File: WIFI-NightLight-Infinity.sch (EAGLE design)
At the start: 34 parts, among them CN1 PBS-3-VERTICAL, CN2 PBS-2-VERTICAL, CN5 PBS-2-VERTICAL, CN6 PBS-2-VERTICAL, CN7 PBS-4-VERTICAL, IC3 MC34063AD, IC4 DS1307Z, M1 ESP8266-12F, Q1 32.768K

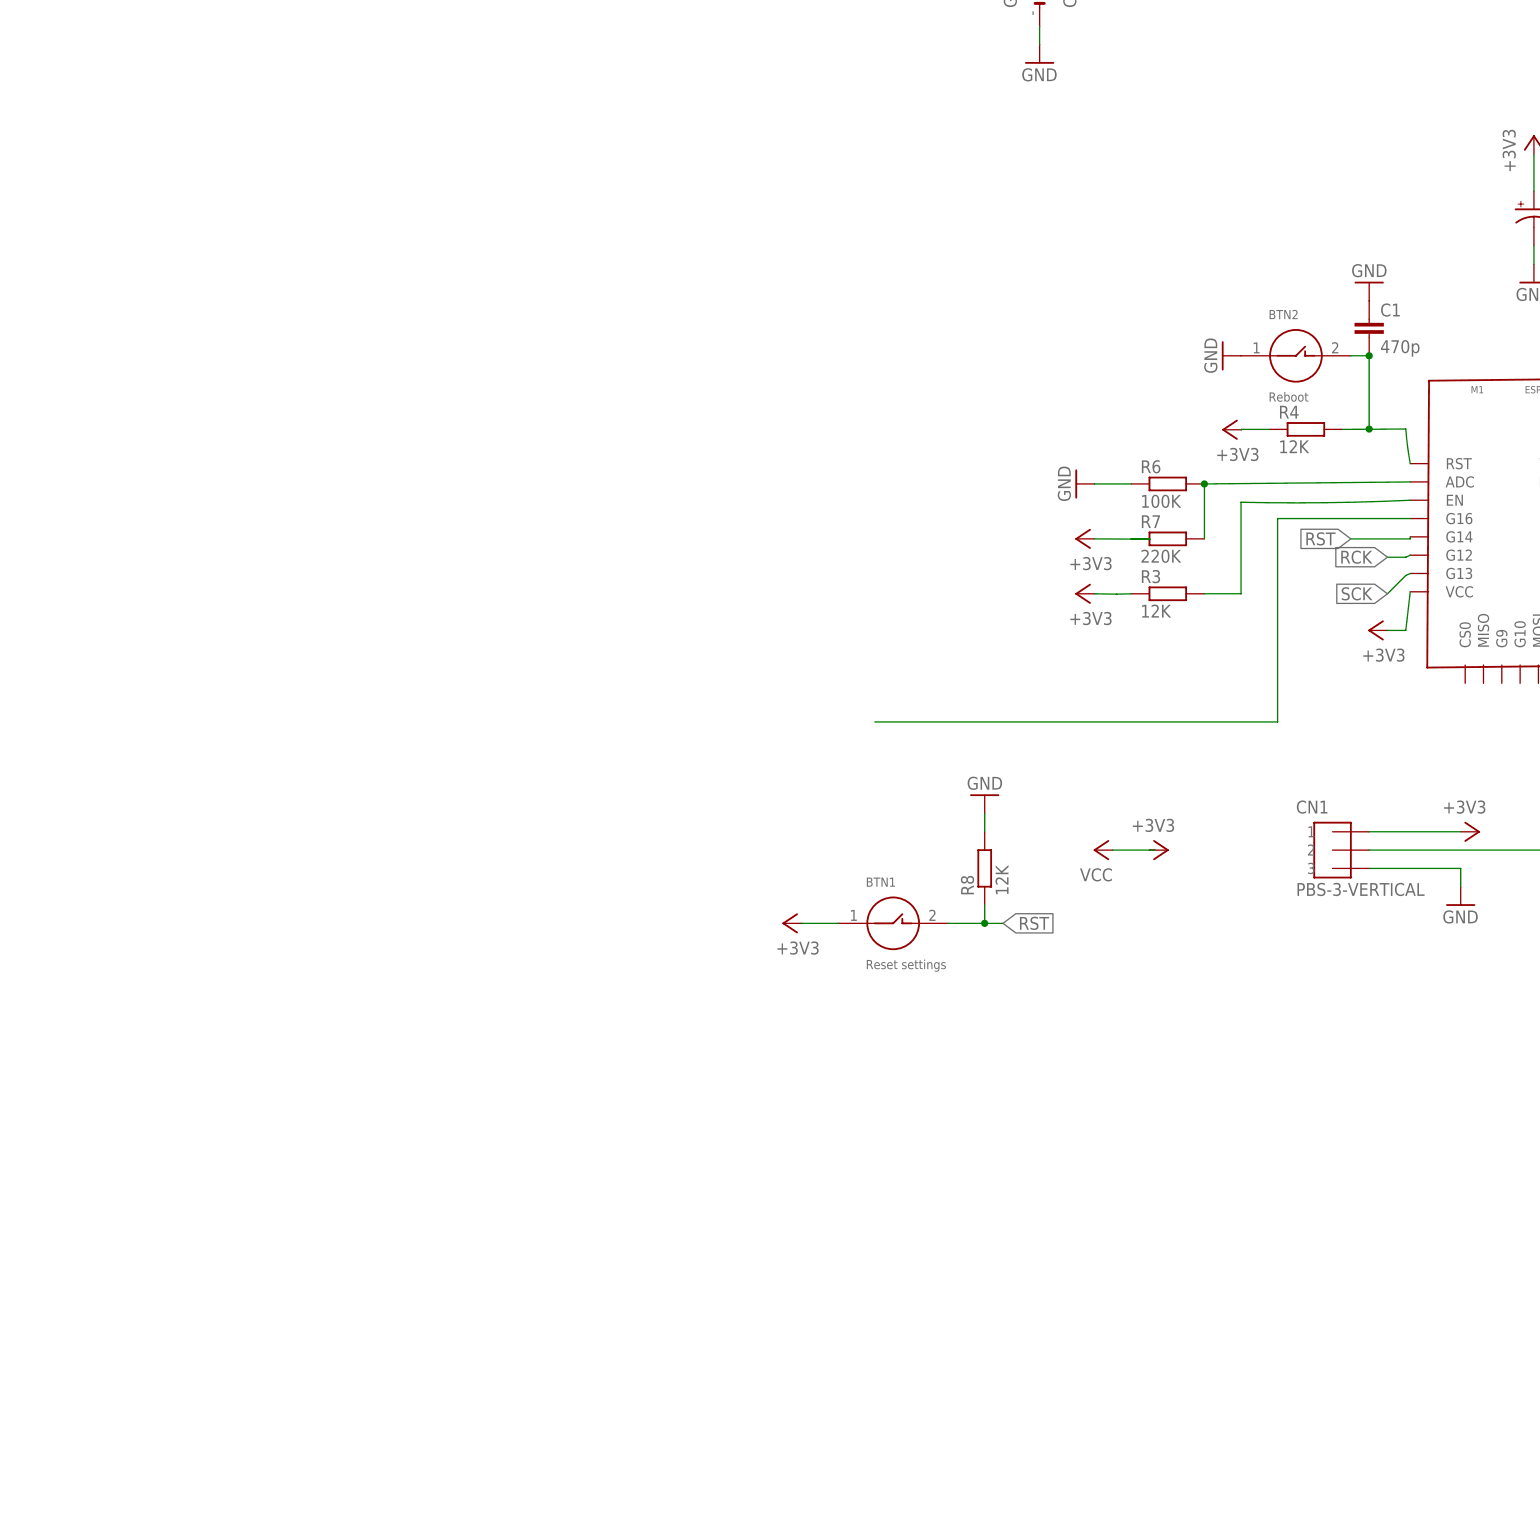
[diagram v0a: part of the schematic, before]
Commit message: transistors were aaded
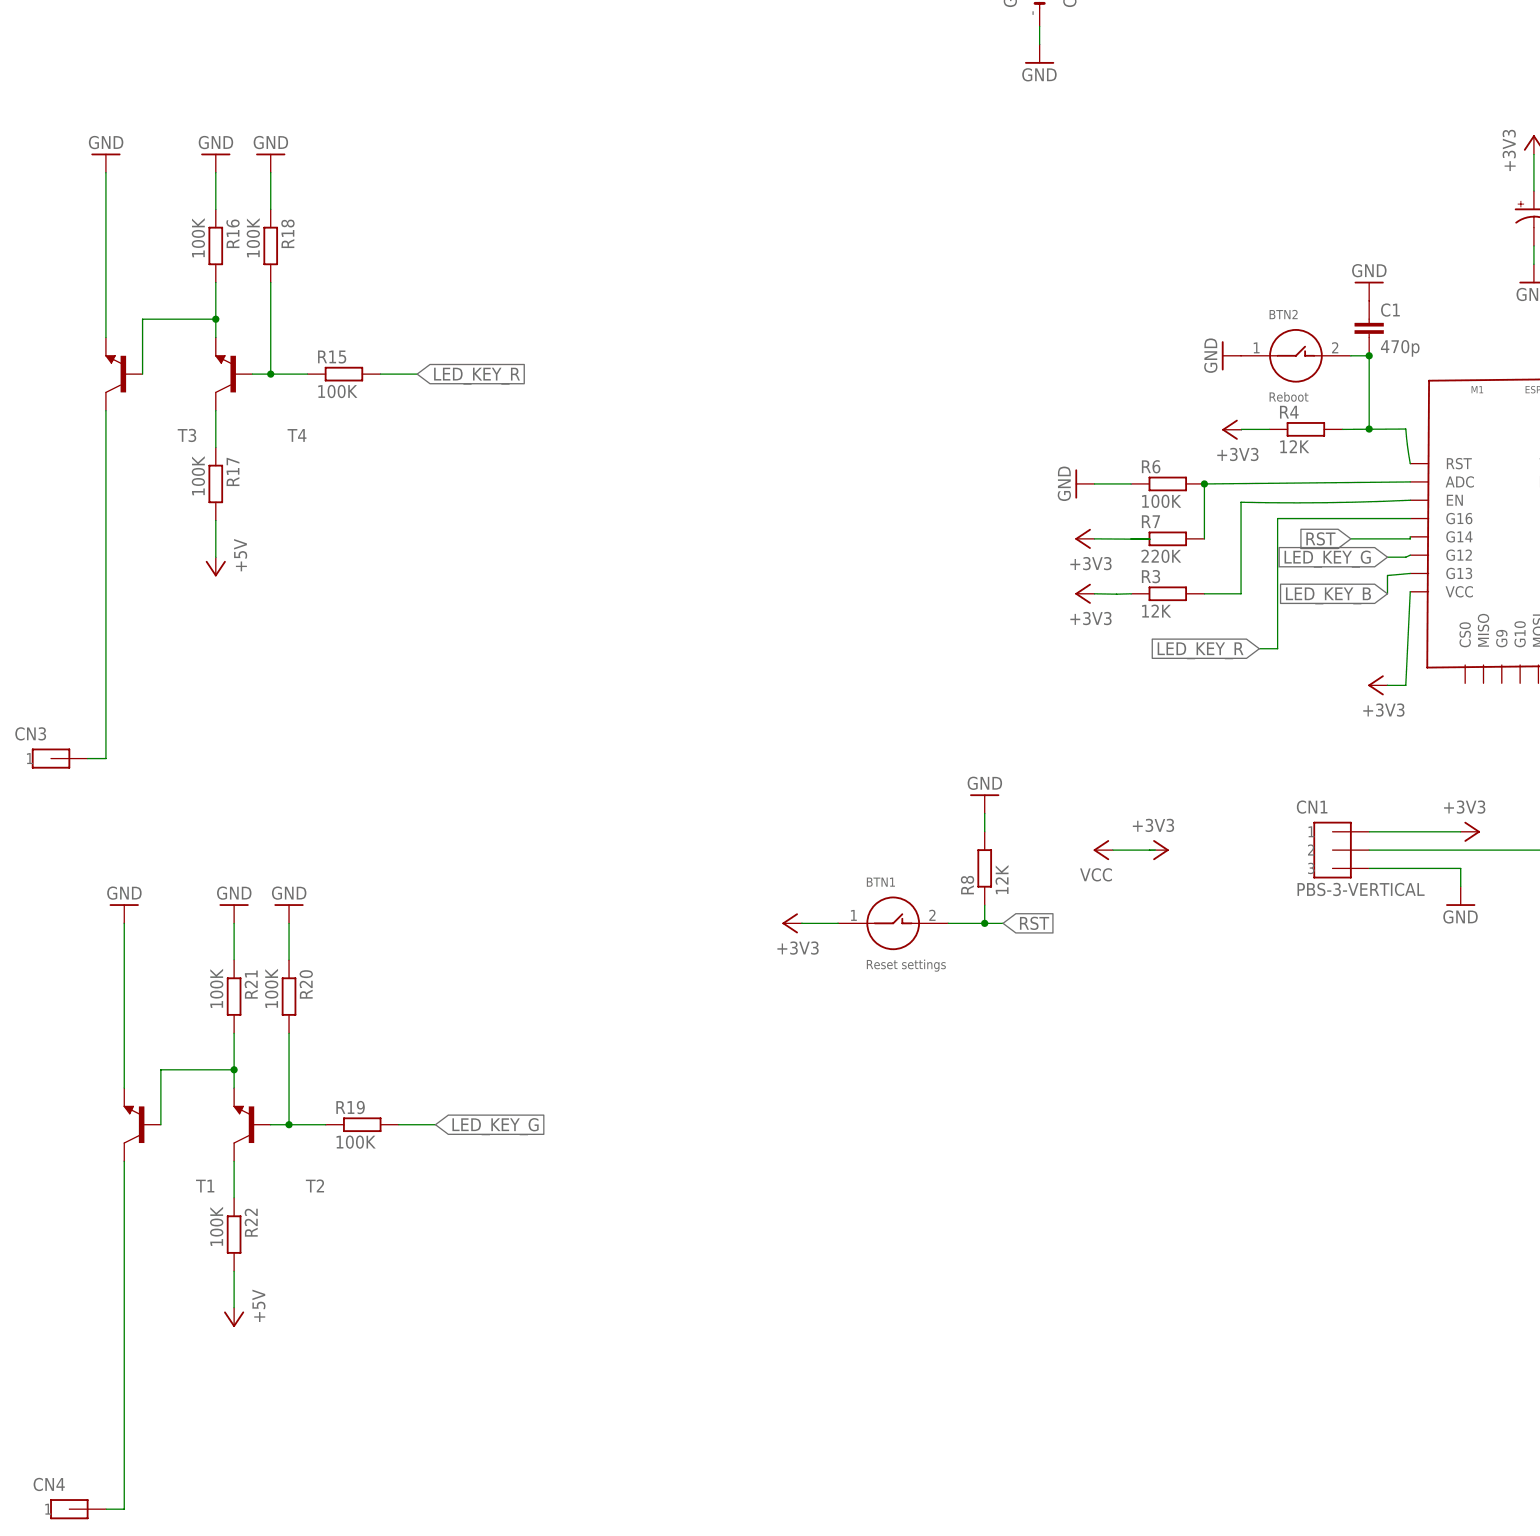
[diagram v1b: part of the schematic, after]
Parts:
- added CN3, CN4: (no value), pls:PBS-1-VERTICAL
- added R15, R16, R17, R18, R19, R20, R21, R22: 100K, eagle-ltspice:RR0603
- added T1, T2, T3, T4: (no value), transistor:-NPN-TO126V
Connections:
- net SCK renamed LED_KEY_B
- removed net N$27: M1.G16
- removed net RCK: M1.G12
- new net LED_KEY_G: M1.G12, R19.2
- new net LED_KEY_R: M1.G16, R15.2
- new net N$10: R17.1, T4.C
- new net N$11: R19.1, R20.2, T2.B
- new net N$12: CN3.1, T3.C
- new net N$13: R21.2, T1.B, T2.E
- new net N$14: R22.1, T2.C
- new net N$15: CN4.1, T1.C
- new net N$8: R15.1, R18.2, T4.B
- new net N$9: R16.2, T3.B, T4.E
- net +5V: now also R17.2, R22.2
- net GND: now also R16.1, R18.1, R20.1, R21.1, T1.E, T3.E

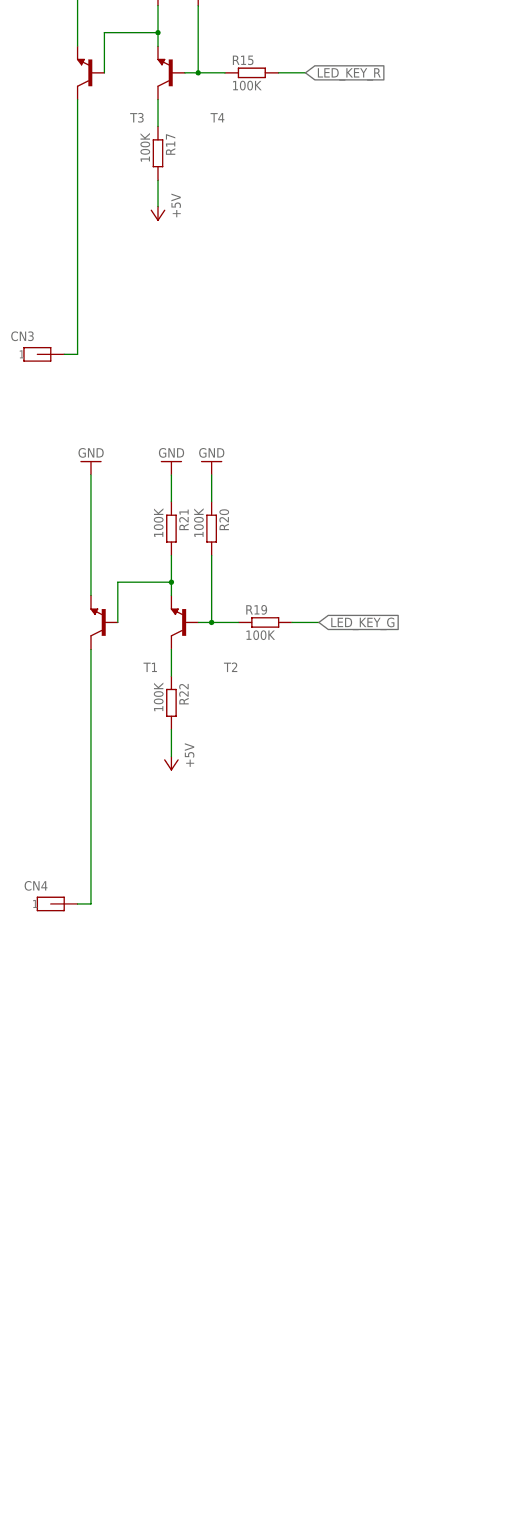
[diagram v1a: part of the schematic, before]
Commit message: Scheme for all led-channels have done
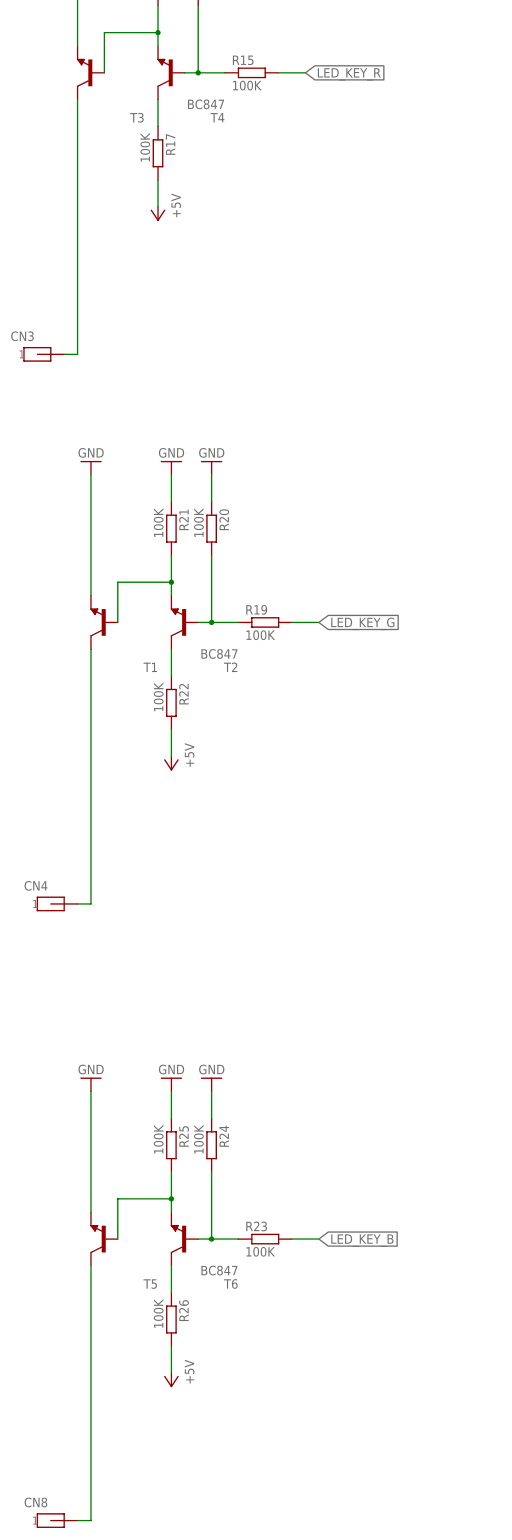
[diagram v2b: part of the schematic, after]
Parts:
- added CN8: (no value), pls:PBS-1-VERTICAL
- added R23, R24, R25, R26: 100K, eagle-ltspice:RR0603
- added T5: (no value), transistor:-NPN-TO126V
- added T6: BC847, transistor:BC847
- T2, T4: value (none) -> BC847; device transistor:-NPN-TO126V -> transistor:BC847
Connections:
- new net N$16: R23.1, R24.2, T6.B
- new net N$17: R25.2, T5.B, T6.E
- new net N$18: R26.1, T6.C
- new net N$19: CN8.1, T5.C
- net +5V: now also R26.2
- net GND: now also R24.1, R25.1, T5.E
- net LED_KEY_B: now also R23.2
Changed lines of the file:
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@@
 <part name="GND21" library="supply1" library_urn="urn:adsk.eagle:library:371" deviceset="GND" device=""/>
 <part name="T3" library="transistor" library_urn="urn:adsk.eagle:library:402" deviceset="*-NPN-" device="TO126V" package3d_urn="urn:adsk.eagle:package:29912/1"/>
-<part name="T4" library="transistor" library_urn="urn:adsk.eagle:library:402" deviceset="*-NPN-" device="TO126V" package3d_urn="urn:adsk.eagle:package:29912/1"/>
+<part name="T4" library="transistor" library_urn="urn:adsk.eagle:library:402" deviceset="BC847" device="" package3d_urn="urn:adsk.eagle:package:29904/2"/>
 <part name="R15" library="eagle-ltspice" library_urn="urn:adsk.eagle:library:217" deviceset="R" device="R0603" package3d_urn="urn:adsk.eagle:package:13302/1" value="100K"/>
 <part name="R18" library="eagle-ltspice" library_urn="urn:adsk.eagle:library:217" deviceset="R" device="R0603" package3d_urn="urn:adsk.eagle:package:13302/1" value="100K"/>
@@
 <part name="CN3" library="pls" deviceset="PBS-1-VERTICAL" device=""/>
 <part name="T1" library="transistor" library_urn="urn:adsk.eagle:library:402" deviceset="*-NPN-" device="TO126V" package3d_urn="urn:adsk.eagle:package:29912/1"/>
-<part name="T2" library="transistor" library_urn="urn:adsk.eagle:library:402" deviceset="*-NPN-" device="TO126V" package3d_urn="urn:adsk.eagle:package:29912/1"/>
+<part name="T2" library="transistor" library_urn="urn:adsk.eagle:library:402" deviceset="BC847" device="" package3d_urn="urn:adsk.eagle:package:29904/2"/>
 <part name="R19" library="eagle-ltspice" library_urn="urn:adsk.eagle:library:217" deviceset="R" device="R0603" package3d_urn="urn:adsk.eagle:package:13302/1" value="100K"/>
 <part name="R20" library="eagle-ltspice" library_urn="urn:adsk.eagle:library:217" deviceset="R" device="R0603" package3d_urn="urn:adsk.eagle:package:13302/1" value="100K"/>
@@
 <part name="P+4" library="supply1" library_urn="urn:adsk.eagle:library:371" deviceset="+5V" device=""/>
 <part name="CN4" library="pls" deviceset="PBS-1-VERTICAL" device=""/>
+<part name="T5" library="transistor" library_urn="urn:adsk.eagle:library:402" deviceset="*-NPN-" device="TO126V" package3d_urn="urn:adsk.eagle:package:29912/1"/>
+<part name="T6" library="transistor" library_urn="urn:adsk.eagle:library:402" deviceset="BC847" device="" package3d_urn="urn:adsk.eagle:package:29904/2"/>
+<part name="R23" library="eagle-ltspice" library_urn="urn:adsk.eagle:library:217" deviceset="R" device="R0603" package3d_urn="urn:adsk.eagle:package:13302/1" value="100K"/>
+<part name="R24" library="eagle-ltspice" library_urn="urn:adsk.eagle:library:217" deviceset="R" device="R0603" package3d_urn="urn:adsk.eagle:package:13302/1" value="100K"/>
+<part name="GND26" library="supply1" library_urn="urn:adsk.eagle:library:371" deviceset="GND" device=""/>
+<part name="GND27" library="supply1" library_urn="urn:adsk.eagle:library:371" deviceset="GND" device=""/>
+<part name="R25" library="eagle-ltspice" library_urn="urn:adsk.eagle:library:217" deviceset="R" device="R0603" package3d_urn="urn:adsk.eagle:package:13302/1" value="100K"/>
+<part name="GND28" library="supply1" library_urn="urn:adsk.eagle:library:371" deviceset="GND" device=""/>
+<part name="R26" library="eagle-ltspice" library_urn="urn:adsk.eagle:library:217" deviceset="R" device="R0603" package3d_urn="urn:adsk.eagle:package:13302/1" value="100K"/>
+<part name="P+6" library="supply1" library_urn="urn:adsk.eagle:library:371" deviceset="+5V" device=""/>
+<part name="CN8" library="pls" deviceset="PBS-1-VERTICAL" device=""/>
 </parts>
 <sheets>
@@
 <instance part="P+4" gate="1" x="-175.26" y="-114.3" rot="R180"/>
 <instance part="CN4" gate="G$1" x="-198.12" y="-139.7"/>
+<instance part="T5" gate="G$1" x="-187.96" y="-203.2" rot="R180"/>
+<instance part="T6" gate="G$1" x="-172.72" y="-203.2" rot="R180"/>
+<instance part="R23" gate="G$1" x="-157.48" y="-203.2"/>
+<instance part="R24" gate="G$1" x="-167.64" y="-185.42" rot="R270"/>
+<instance part="GND26" gate="1" x="-167.64" y="-172.72" rot="R180"/>
+<instance part="GND27" gate="1" x="-190.5" y="-172.72" rot="R180"/>
+<instance part="R25" gate="G$1" x="-175.26" y="-185.42" rot="R270"/>
+<instance part="GND28" gate="1" x="-175.26" y="-172.72" rot="R180"/>
+<instance part="R26" gate="G$1" x="-175.26" y="-218.44" rot="R270"/>
+<instance part="P+6" gate="1" x="-175.26" y="-231.14" rot="R180"/>
+<instance part="CN8" gate="G$1" x="-198.12" y="-256.54"/>
 </instances>
 <busses>
@@
 <pinref part="GND24" gate="1" pin="GND"/>
 <wire x1="-190.5" y1="-58.42" x2="-190.5" y2="-81.28" width="0.1524" layer="91"/>
+</segment>
+<segment>
+<pinref part="R24" gate="G$1" pin="1"/>
+<pinref part="GND26" gate="1" pin="GND"/>
+<wire x1="-167.64" y1="-175.26" x2="-167.64" y2="-180.34" width="0.1524" layer="91"/>
+</segment>
+<segment>
+<pinref part="R25" gate="G$1" pin="1"/>
+<pinref part="GND28" gate="1" pin="GND"/>
+<wire x1="-175.26" y1="-175.26" x2="-175.26" y2="-180.34" width="0.1524" layer="91"/>
+</segment>
+<segment>
+<pinref part="T5" gate="G$1" pin="E"/>
+<pinref part="GND27" gate="1" pin="GND"/>
+<wire x1="-190.5" y1="-175.26" x2="-190.5" y2="-198.12" width="0.1524" layer="91"/>
 </segment>
 </net>
@@
 <label x="-15.24" y="-12.7" size="1.778" layer="95" rot="R180" xref="yes"/>
 </segment>
+<segment>
+<wire x1="-152.4" y1="-203.2" x2="-147.32" y2="-203.2" width="0.1524" layer="91"/>
+<label x="-147.32" y="-203.2" size="1.778" layer="95" xref="yes"/>
+<pinref part="R23" gate="G$1" pin="2"/>
+</segment>
 </net>
 <net name="LED_KEY_R" class="0">
@@
 <pinref part="P+4" gate="1" pin="+5V"/>
 <wire x1="-175.26" y1="-111.76" x2="-175.26" y2="-106.68" width="0.1524" layer="91"/>
+</segment>
+<segment>
+<pinref part="R26" gate="G$1" pin="2"/>
+<pinref part="P+6" gate="1" pin="+5V"/>
+<wire x1="-175.26" y1="-228.6" x2="-175.26" y2="-223.52" width="0.1524" layer="91"/>
 </segment>
 </net>
@@
 </segment>
 </net>
+<net name="N$16" class="0">
+<segment>
+<pinref part="T6" gate="G$1" pin="B"/>
+<pinref part="R23" gate="G$1" pin="1"/>
+<wire x1="-162.56" y1="-203.2" x2="-167.64" y2="-203.2" width="0.1524" layer="91"/>
+<pinref part="R24" gate="G$1" pin="2"/>
+<wire x1="-167.64" y1="-203.2" x2="-170.18" y2="-203.2" width="0.1524" layer="91"/>
+<wire x1="-167.64" y1="-190.5" x2="-167.64" y2="-203.2" width="0.1524" layer="91"/>
+<junction x="-167.64" y="-203.2"/>
+</segment>
+</net>
+<net name="N$17" class="0">
+<segment>
+<pinref part="T6" gate="G$1" pin="E"/>
+<pinref part="R25" gate="G$1" pin="2"/>
+<wire x1="-175.26" y1="-190.5" x2="-175.26" y2="-195.58" width="0.1524" layer="91"/>
+<pinref part="T5" gate="G$1" pin="B"/>
+<wire x1="-175.26" y1="-195.58" x2="-175.26" y2="-198.12" width="0.1524" layer="91"/>
+<wire x1="-185.42" y1="-203.2" x2="-185.42" y2="-195.58" width="0.1524" layer="91"/>
+<wire x1="-185.42" y1="-195.58" x2="-175.26" y2="-195.58" width="0.1524" layer="91"/>
+<junction x="-175.26" y="-195.58"/>
+</segment>
+</net>
+<net name="N$18" class="0">
+<segment>
+<pinref part="T6" gate="G$1" pin="C"/>
+<pinref part="R26" gate="G$1" pin="1"/>
+<wire x1="-175.26" y1="-213.36" x2="-175.26" y2="-208.28" width="0.1524" layer="91"/>
+</segment>
+</net>
+<net name="N$19" class="0">
+<segment>
+<pinref part="T5" gate="G$1" pin="C"/>
+<wire x1="-193.04" y1="-256.54" x2="-190.5" y2="-256.54" width="0.1524" layer="91"/>
+<wire x1="-190.5" y1="-256.54" x2="-190.5" y2="-208.28" width="0.1524" layer="91"/>
+<pinref part="CN8" gate="G$1" pin="1"/>
+</segment>
+</net>
